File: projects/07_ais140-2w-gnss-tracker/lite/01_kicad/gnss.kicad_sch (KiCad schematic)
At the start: 18 parts, among them J5 GNSS ANT, Q3 BSS138, Q4 BSS138, U5 L76K, U6 AP2112K-3.3

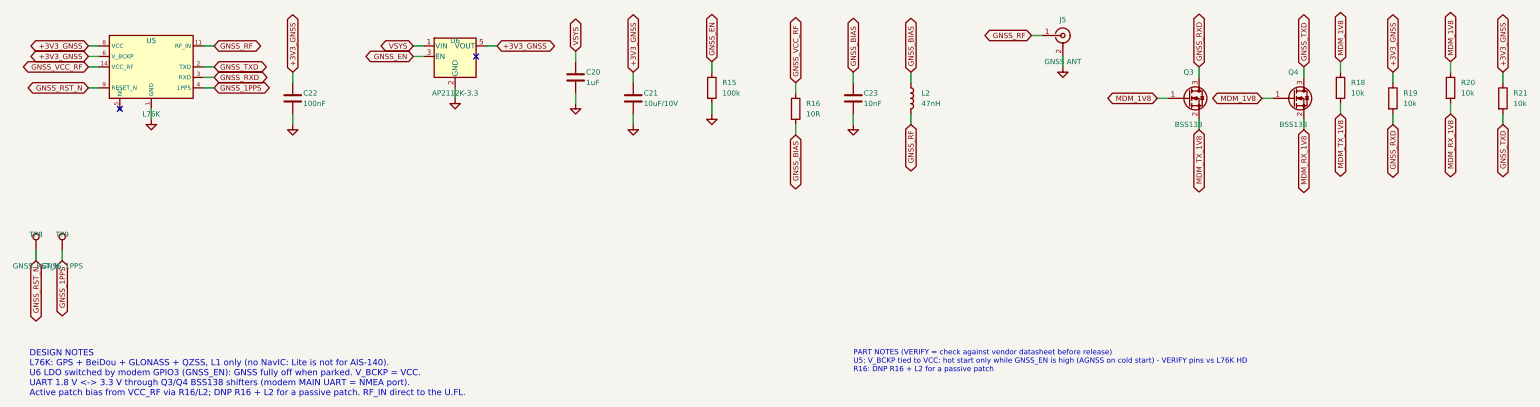
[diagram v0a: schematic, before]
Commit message: Tracker 07 Lite (WIP): L-match LTE, passive GNSS patch, bottom test pads, fab script
Co-Authored-By: Claude Opus 5.5 <noreply@anthropic.com>
Claude-Session: https://claude.ai/code/session_01Hk6s8R6up8HYVQWXd3atVk
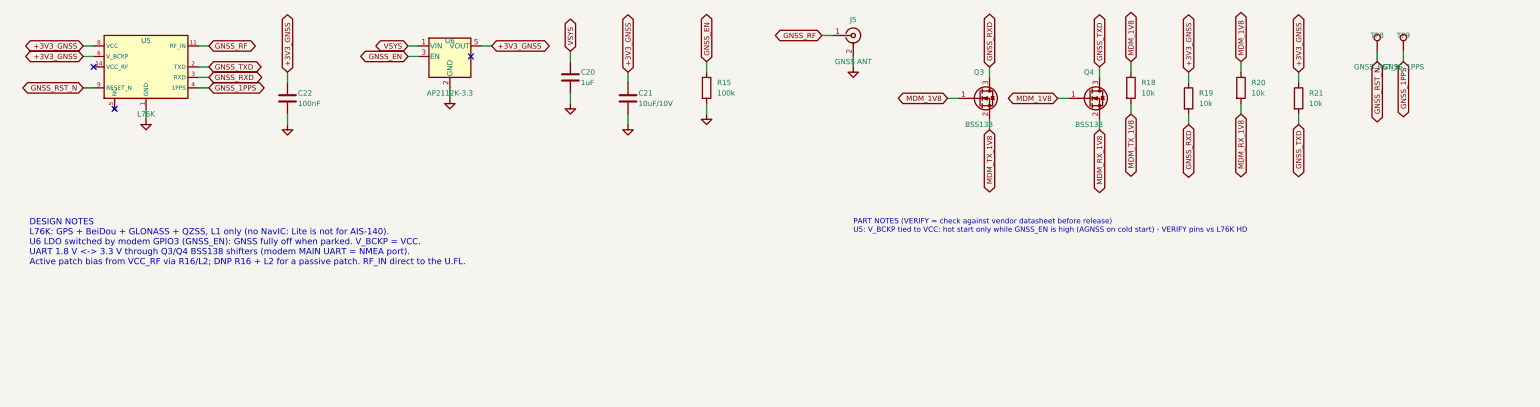
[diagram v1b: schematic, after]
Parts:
- removed C23: 10nF, Capacitor_SMD:C_0402_1005Metric, symbol Device:C
- removed L2: 47nH, Inductor_SMD:L_0402_1005Metric, symbol Device:L
- removed R16: 10R, Resistor_SMD:R_0402_1005Metric, symbol Device:R
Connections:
- net GNSS_VCC_RF: no longer names the net of U5.14 (VCC_RF)
- no-connect marks 2 -> 3
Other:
- note added: "PART NOTES (VERIFY = check against vendor datasheet before release) U5: V_BCKP tied to VCC: hot start only while GNSS_EN is high (AGNSS on cold start) - VERIFY pins vs L76K HD"
- note removed: "PART NOTES (VERIFY = check against vendor datasheet before release) U5: V_BCKP tied to VCC: hot start only while GNSS_EN is high (AGNSS on cold start) - VERIFY pins vs L76K HD R16: DNP R16 + L2 for a passive patch"
- moved on the sheet: C20, C21, C22, J5, Q3, Q4, R15, R18, R19, R20, R21, TP8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
